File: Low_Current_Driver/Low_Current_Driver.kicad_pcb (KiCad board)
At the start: 4 copper layers, 160 x 99.5 mm, 194 parts, among them J1 Conn_01x02, J2 RJ45, J3 Screw_Terminal_01x04, J4 Conn_02x07_Odd_Even, J5 Channel 3, J6 Channel 2, J7 Channel 1, J8 MS548-10F, J9 Conn_01x02, Q1 Si4447ADY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

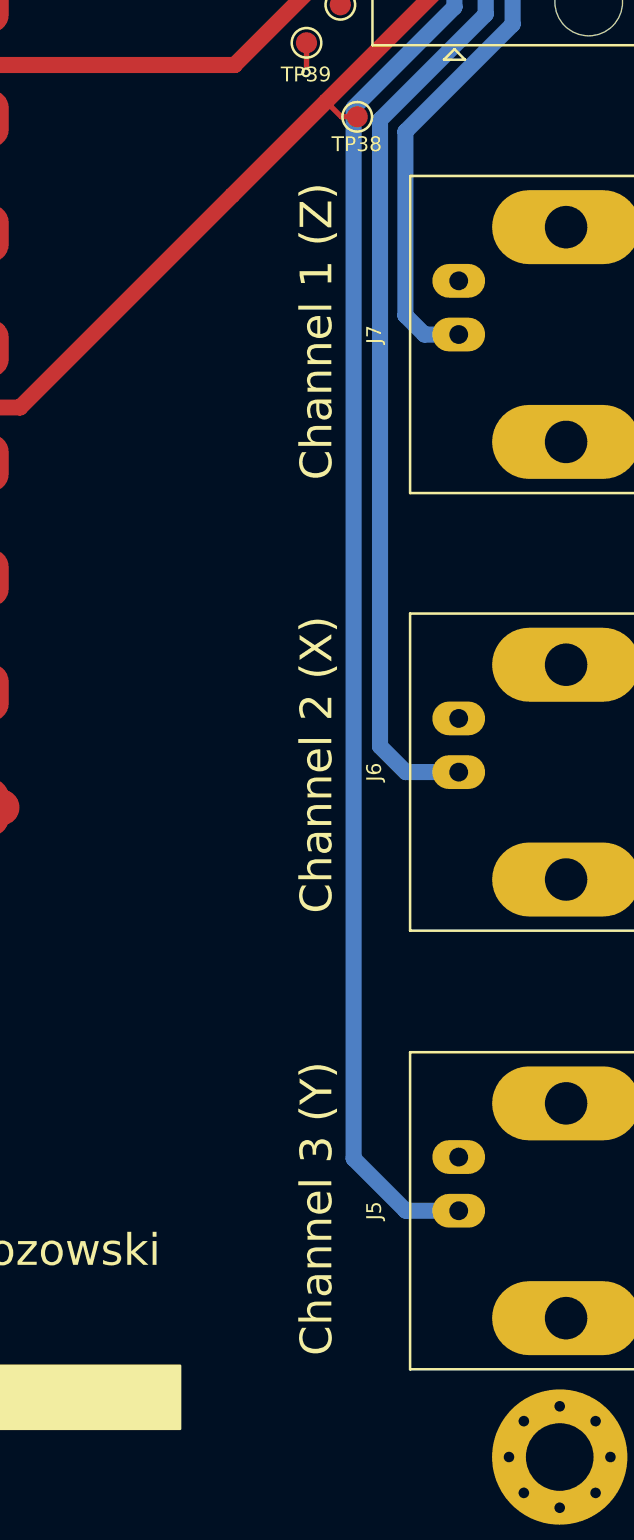
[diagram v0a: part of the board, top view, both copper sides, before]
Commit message: Silkscreen update LCD
Removed EQOP specific "X" "Y" "Z" from the channels
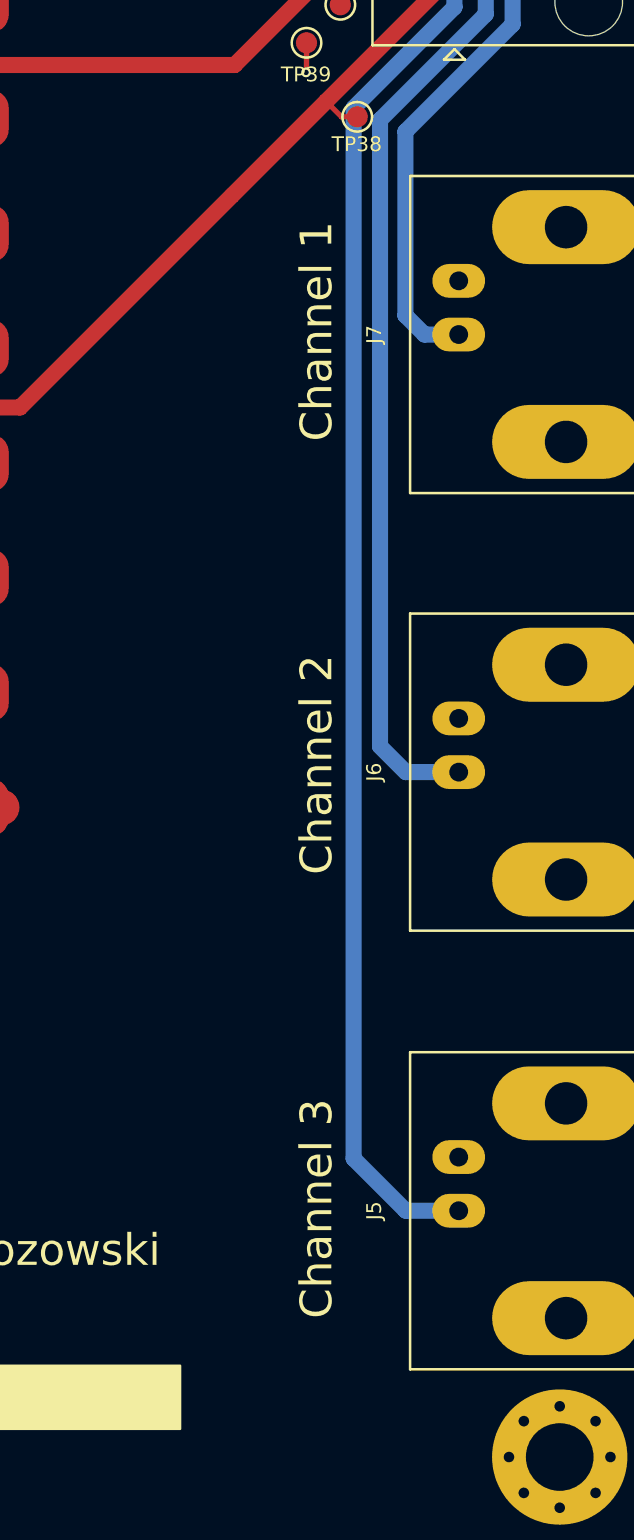
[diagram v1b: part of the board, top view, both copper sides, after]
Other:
- board text removed: "Channel 1 (Z)"
- board text removed: "Channel 2 (X)"
- board text removed: "Channel 3 (Y)"

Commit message: HCD amplifier update
- Updated OPA2277 amplifiers to OPA2210 that were actually populated on the boards.
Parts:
- U10, U11, U12, U13, U14, U9: value OPA2277 -> OPA2210
